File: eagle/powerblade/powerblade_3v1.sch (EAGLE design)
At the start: 94 parts, among them J1 JTAG_14PIN_IDC-NL, J21 AC_INSLOT2, J4 TC2030-JLINK-NL, Q1 2N7002, Q3 2SK1829, Q4 2SK1829, U1 TPS62122, U2 MCP6V3, U3 MSP430FR5738, U4 NRF51822QF, U6 MAX9910, U7 OPA2369, X1 16MHz, X3 32.768kHz, Y1 UREACH_XTEND

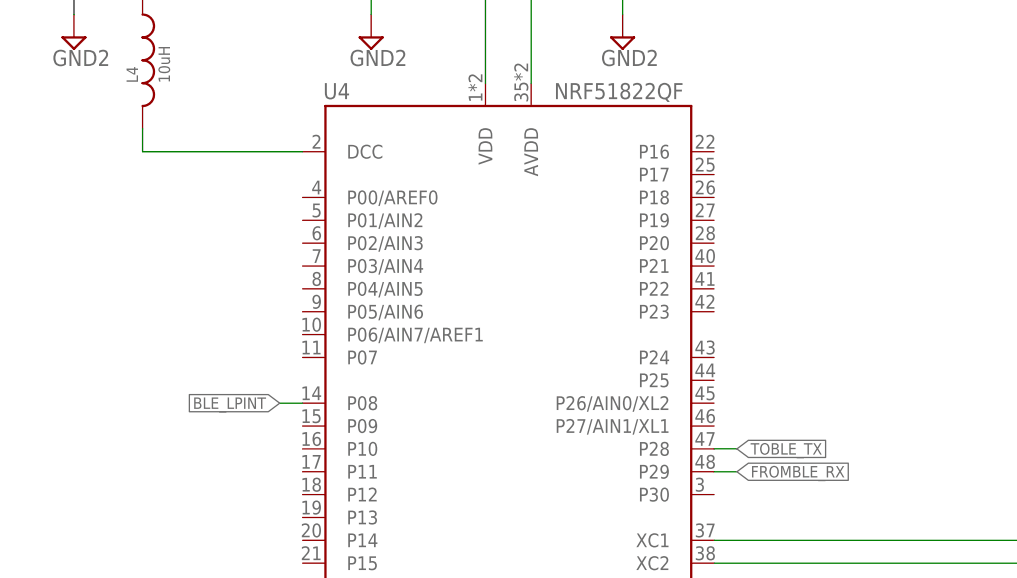
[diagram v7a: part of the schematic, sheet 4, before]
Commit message: more routing in powerblade
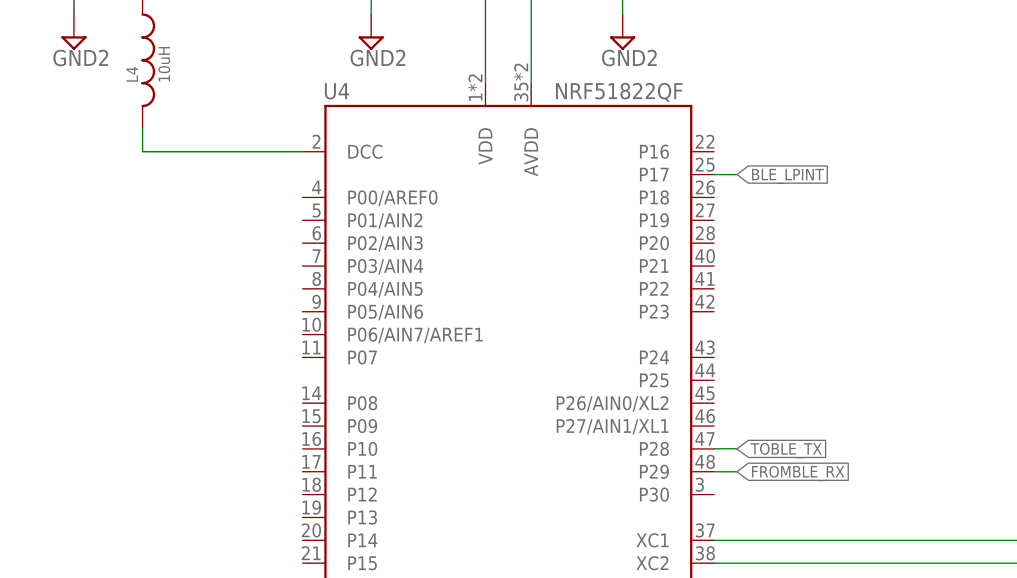
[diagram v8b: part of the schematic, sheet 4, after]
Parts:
- R23, R6: device rcl:R-US_R0603_SM -> rcl:R-US_R0402_SM
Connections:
- removed net N$2: D1.C, D2.A, R3.2
- net BLE_LPINT: now also U4.P17; no longer U4.P08
- net ZC: now also D1.C, D2.A, R3.2
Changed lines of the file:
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@@
 <grid distance="0.1" unitdist="inch" unit="inch" style="lines" multiple="1" display="no" altdistance="0.01" altunitdist="inch" altunit="inch"/>
 <layers>
-<layer number="1" name="Top" color="4" fill="1" visible="no" active="no"/>
-<layer number="2" name="Route2" color="1" fill="3" visible="no" active="no"/>
-<layer number="3" name="Route3" color="4" fill="3" visible="no" active="no"/>
-<layer number="4" name="Route4" color="1" fill="4" visible="no" active="no"/>
-<layer number="5" name="Route5" color="4" fill="4" visible="no" active="no"/>
-<layer number="6" name="Route6" color="1" fill="8" visible="no" active="no"/>
-<layer number="7" name="Route7" color="4" fill="8" visible="no" active="no"/>
-<layer number="8" name="Route8" color="1" fill="2" visible="no" active="no"/>
-<layer number="9" name="Route9" color="4" fill="2" visible="no" active="no"/>
-<layer number="10" name="Route10" color="1" fill="7" visible="no" active="no"/>
-<layer number="11" name="Route11" color="4" fill="7" visible="no" active="no"/>
-<layer number="12" name="Route12" color="1" fill="5" visible="no" active="no"/>
-<layer number="13" name="Route13" color="4" fill="5" visible="no" active="no"/>
-<layer number="14" name="Route14" color="1" fill="6" visible="no" active="no"/>
-<layer number="15" name="Route15" color="4" fill="6" visible="no" active="no"/>
-<layer number="16" name="Bottom" color="1" fill="1" visible="no" active="no"/>
-<layer number="17" name="Pads" color="2" fill="1" visible="no" active="no"/>
-<layer number="18" name="Vias" color="2" fill="1" visible="no" active="no"/>
-<layer number="19" name="Unrouted" color="6" fill="1" visible="no" active="no"/>
-<layer number="20" name="Dimension" color="15" fill="1" visible="no" active="no"/>
-<layer number="21" name="tPlace" color="7" fill="1" visible="no" active="no"/>
-<layer number="22" name="bPlace" color="7" fill="1" visible="no" active="no"/>
-<layer number="23" name="tOrigins" color="15" fill="1" visible="no" active="no"/>
-<layer number="24" name="bOrigins" color="15" fill="1" visible="no" active="no"/>
-<layer number="25" name="tNames" color="7" fill="1" visible="no" active="no"/>
-<layer number="26" name="bNames" color="7" fill="1" visible="no" active="no"/>
-<layer number="27" name="tValues" color="7" fill="1" visible="no" active="no"/>
-<layer number="28" name="bValues" color="7" fill="1" visible="no" active="no"/>
+<layer number="1" name="Top" color="4" fill="1" visible="yes" active="no"/>
+<layer number="2" name="Route2" color="1" fill="3" visible="yes" active="no"/>
+<layer number="3" name="Route3" color="4" fill="3" visible="yes" active="no"/>
+<layer number="4" name="Route4" color="1" fill="4" visible="yes" active="no"/>
+<layer number="5" name="Route5" color="4" fill="4" visible="yes" active="no"/>
+<layer number="6" name="Route6" color="1" fill="8" visible="yes" active="no"/>
+<layer number="7" name="Route7" color="4" fill="8" visible="yes" active="no"/>
+<layer number="8" name="Route8" color="1" fill="2" visible="yes" active="no"/>
+<layer number="9" name="Route9" color="4" fill="2" visible="yes" active="no"/>
+<layer number="10" name="Route10" color="1" fill="7" visible="yes" active="no"/>
+<layer number="11" name="Route11" color="4" fill="7" visible="yes" active="no"/>
+<layer number="12" name="Route12" color="1" fill="5" visible="yes" active="no"/>
+<layer number="13" name="Route13" color="4" fill="5" visible="yes" active="no"/>
+<layer number="14" name="Route14" color="1" fill="6" visible="yes" active="no"/>
+<layer number="15" name="Route15" color="4" fill="6" visible="yes" active="no"/>
+<layer number="16" name="Bottom" color="1" fill="1" visible="yes" active="no"/>
+<layer number="17" name="Pads" color="2" fill="1" visible="yes" active="no"/>
+<layer number="18" name="Vias" color="2" fill="1" visible="yes" active="no"/>
+<layer number="19" name="Unrouted" color="6" fill="1" visible="yes" active="no"/>
+<layer number="20" name="Dimension" color="15" fill="1" visible="yes" active="no"/>
+<layer number="21" name="tPlace" color="7" fill="1" visible="yes" active="no"/>
+<layer number="22" name="bPlace" color="7" fill="1" visible="yes" active="no"/>
+<layer number="23" name="tOrigins" color="15" fill="1" visible="yes" active="no"/>
+<layer number="24" name="bOrigins" color="15" fill="1" visible="yes" active="no"/>
+<layer number="25" name="tNames" color="7" fill="1" visible="yes" active="no"/>
+<layer number="26" name="bNames" color="7" fill="1" visible="yes" active="no"/>
+<layer number="27" name="tValues" color="7" fill="1" visible="yes" active="no"/>
+<layer number="28" name="bValues" color="7" fill="1" visible="yes" active="no"/>
 <layer number="29" name="tStop" color="7" fill="3" visible="no" active="no"/>
 <layer number="30" name="bStop" color="7" fill="6" visible="no" active="no"/>
@@
 <layer number="35" name="tGlue" color="7" fill="4" visible="no" active="no"/>
 <layer number="36" name="bGlue" color="7" fill="5" visible="no" active="no"/>
-<layer number="37" name="tTest" color="7" fill="1" visible="no" active="no"/>
-<layer number="38" name="bTest" color="7" fill="1" visible="no" active="no"/>
+<layer number="37" name="tTest" color="7" fill="1" visible="yes" active="no"/>
+<layer number="38" name="bTest" color="7" fill="1" visible="yes" active="no"/>
 <layer number="39" name="tKeepout" color="4" fill="11" visible="no" active="no"/>
 <layer number="40" name="bKeepout" color="1" fill="11" visible="no" active="no"/>
@@
 <layer number="44" name="Drills" color="7" fill="1" visible="no" active="no"/>
 <layer number="45" name="Holes" color="7" fill="1" visible="no" active="no"/>
-<layer number="46" name="Milling" color="3" fill="1" visible="no" active="no"/>
-<layer number="47" name="Measures" color="7" fill="1" visible="no" active="no"/>
-<layer number="48" name="Document" color="7" fill="1" visible="no" active="no"/>
-<layer number="49" name="Reference" color="7" fill="1" visible="no" active="no"/>
-<layer number="50" name="dxf" color="7" fill="1" visible="no" active="no"/>
-<layer number="51" name="tDocu" color="7" fill="1" visible="no" active="no"/>
-<layer number="52" name="bDocu" color="7" fill="1" visible="no" active="no"/>
-<layer number="53" name="tGND_GNDA" color="7" fill="9" visible="no" active="no"/>
-<layer number="54" name="bGND_GNDA" color="1" fill="9" visible="no" active="no"/>
-<layer number="56" name="wert" color="7" fill="1" visible="no" active="no"/>
-<layer number="57" name="tCAD" color="7" fill="1" visible="no" active="no"/>
+<layer number="46" name="Milling" color="3" fill="1" visible="yes" active="no"/>
+<layer number="47" name="Measures" color="7" fill="1" visible="yes" active="no"/>
+<layer number="48" name="Document" color="7" fill="1" visible="yes" active="no"/>
+<layer number="49" name="Reference" color="7" fill="1" visible="yes" active="no"/>
+<layer number="50" name="dxf" color="7" fill="1" visible="yes" active="no"/>
+<layer number="51" name="tDocu" color="7" fill="1" visible="yes" active="no"/>
+<layer number="52" name="bDocu" color="7" fill="1" visible="yes" active="no"/>
+<layer number="53" name="tGND_GNDA" color="7" fill="9" visible="yes" active="no"/>
+<layer number="54" name="bGND_GNDA" color="1" fill="9" visible="yes" active="no"/>
+<layer number="56" name="wert" color="7" fill="1" visible="yes" active="no"/>
+<layer number="57" name="tCAD" color="7" fill="1" visible="yes" active="no"/>
 <layer number="91" name="Nets" color="2" fill="1" visible="yes" active="yes"/>
 <layer number="92" name="Busses" color="1" fill="1" visible="yes" active="yes"/>
@@
 <attribute name="DIGIKEY" value="160-1183-1-ND"/>
 </part>
-<part name="R23" library="rcl" deviceset="R-US_" device="R0603_SM" value="120">
+<part name="R23" library="rcl" deviceset="R-US_" device="R0402_SM" value="120">
 <attribute name="DIGIKEY" value="P120GCT-ND"/>
 </part>
@@
 <part name="Q4" library="powerfilm" deviceset="2SK1829" device=""/>
 <part name="SUPPLY19" library="supply2" deviceset="GND3" device=""/>
-<part name="R6" library="rcl" deviceset="R-US_" device="R0603_SM" value="660k"/>
+<part name="R6" library="rcl" deviceset="R-US_" device="R0402_SM" value="660k"/>
 <part name="SUPPLY20" library="supply2" deviceset="GND3" device=""/>
 <part name="SUPPLY21" library="supply2" deviceset="GND3" device=""/>
@@
 </segment>
 </net>
-<net name="N$2" class="0">
+<net name="ZC" class="0">
 <segment>
 <pinref part="D1" gate="G$1" pin="C"/>
@@
 <wire x1="71.12" y1="17.78" x2="58.42" y2="17.78" width="0.1524" layer="91"/>
 <junction x="58.42" y="17.78"/>
+<wire x1="53.34" y1="27.94" x2="58.42" y2="27.94" width="0.1524" layer="91"/>
+<wire x1="58.42" y1="27.94" x2="58.42" y2="17.78" width="0.1524" layer="91"/>
+<label x="53.34" y="27.94" size="1.27" layer="95" rot="R180" xref="yes"/>
 </segment>
 </net>
@@
 <net name="BLE_LPINT" class="0">
 <segment>
-<label x="-68.58" y="-10.16" size="1.27" layer="95" rot="R180" xref="yes"/>
-<pinref part="U4" gate="G$1" pin="P08"/>
-<wire x1="-68.58" y1="-10.16" x2="-66.04" y2="-10.16" width="0.1524" layer="91"/>
-</segment>
-</net>
+<label x="-17.78" y="15.24" size="1.27" layer="95" xref="yes"/>
+<pinref part="U4" gate="G$1" pin="P17"/>
+<wire x1="-20.32" y1="15.24" x2="-17.78" y2="15.24" width="0.1524" layer="91"/>
+</segment>
+</net>
